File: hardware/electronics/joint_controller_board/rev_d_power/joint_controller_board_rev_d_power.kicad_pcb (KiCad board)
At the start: 2 copper layers, 40 x 60 mm, 19 parts, among them J1 J_IFACE, J2 J_PWR_IN_RAW, J3 J_PWR_CHAIN_RAW, J4 J_PWR_OUT_SW

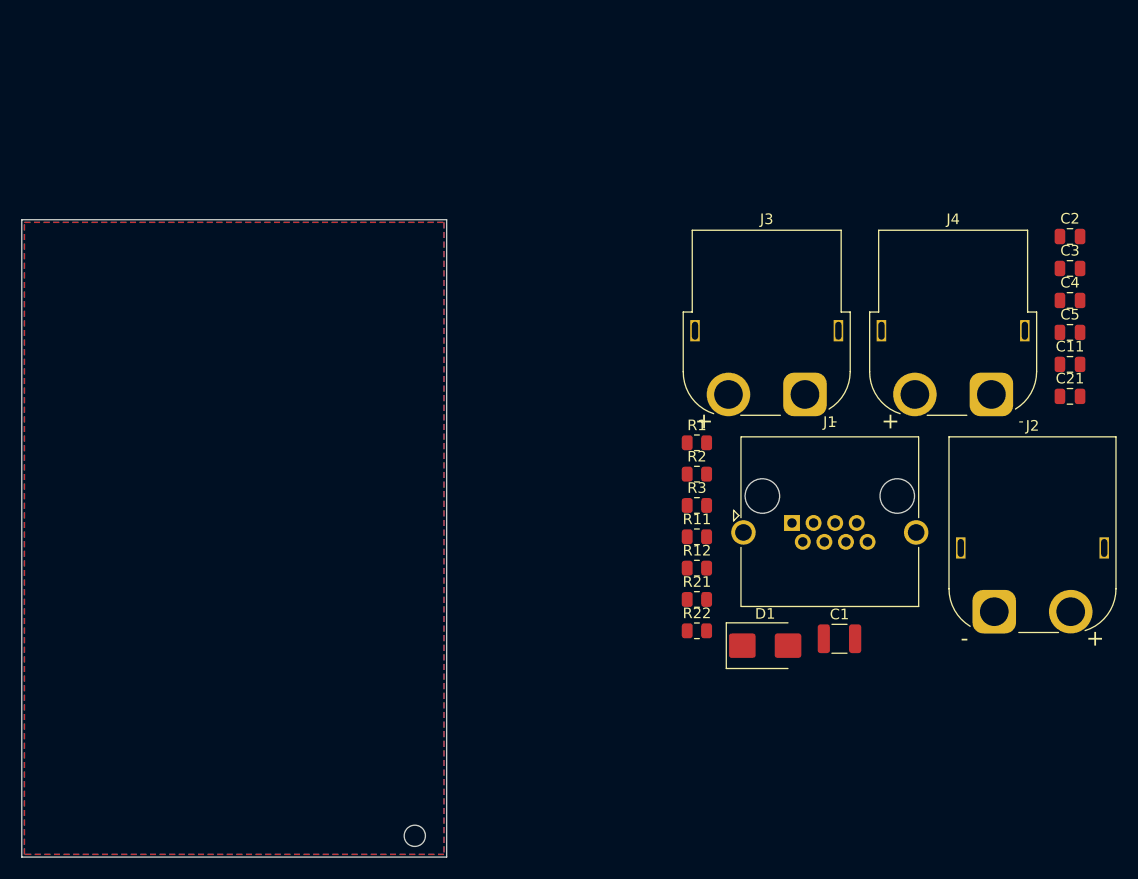
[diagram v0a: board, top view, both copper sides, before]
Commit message: feat: refine rev d power protection and buck
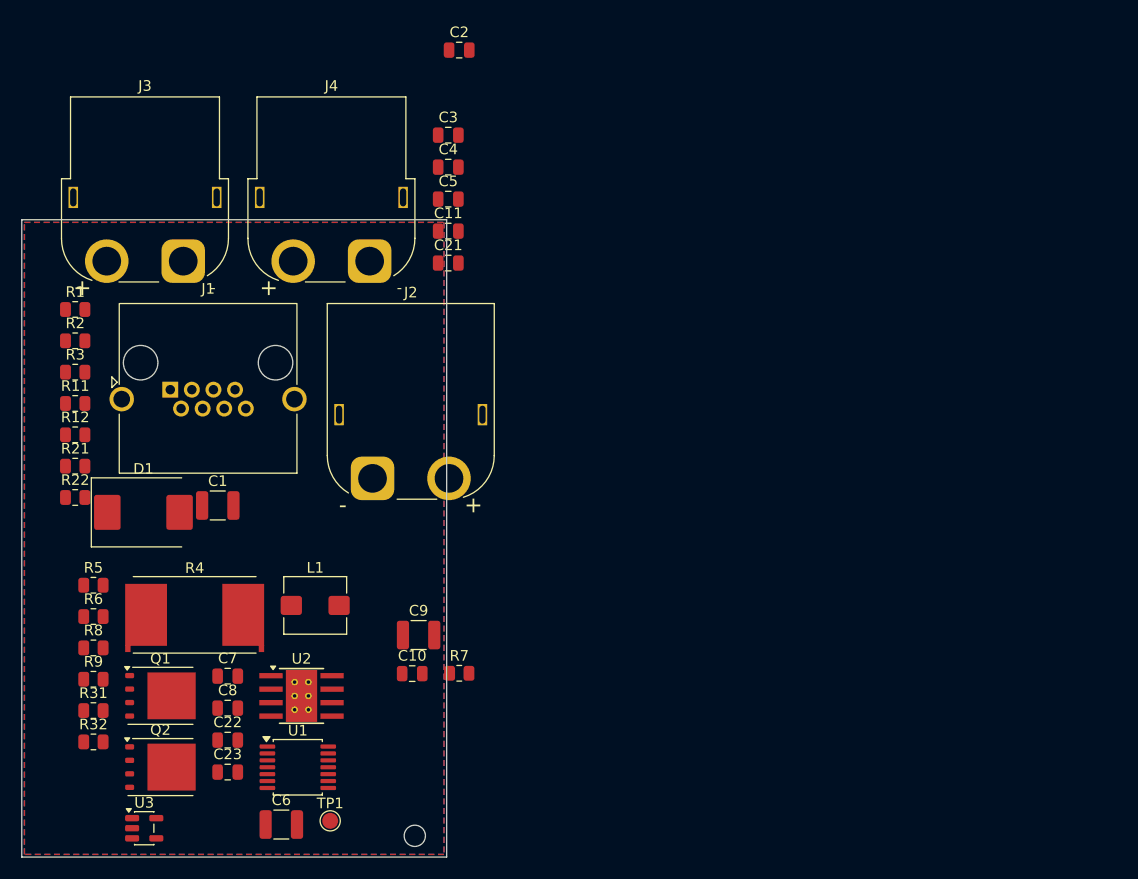
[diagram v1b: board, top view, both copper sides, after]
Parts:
- added C10: 10nF, Capacitor_SMD:C_0805_2012Metric, F.Cu at (156.8, 102.7)
- added C22: 47nF, Capacitor_SMD:C_0805_2012Metric, F.Cu at (139.4, 109.0)
- added C23: 100nF, Capacitor_SMD:C_0805_2012Metric, F.Cu at (139.4, 112.0)
- added C6: 4u7, Capacitor_SMD:C_1210_3225Metric, F.Cu at (144.4, 116.9)
- added C7: 1uF, Capacitor_SMD:C_0805_2012Metric, F.Cu at (139.4, 103.0)
- added C8: 100nF, Capacitor_SMD:C_0805_2012Metric, F.Cu at (139.4, 106.0)
- added C9: 22uF, Capacitor_SMD:C_1210_3225Metric, F.Cu at (157.4, 99.1)
- added L1: 15uH, Inductor_SMD:L_Bourns_SRP5030T, F.Cu at (147.6, 96.3)
- added Q1: BSC016N06NS, Package_TO_SOT_SMD:TDSON-8-1, F.Cu at (133.1, 104.8)
- added Q2: BSC016N06NS, Package_TO_SOT_SMD:TDSON-8-1, F.Cu at (133.1, 111.5)
- added R31: 220k, Resistor_SMD:R_0805_2012Metric, F.Cu at (126.7, 106.2)
- added R32: 10k, Resistor_SMD:R_0805_2012Metric, F.Cu at (126.7, 109.2)
- added R4: 1.25mOhm, Resistor_SMD:R_Shunt_Vishay_WSR2_WSR3_KelvinConnection, F.Cu at (136.3, 97.5)
- added R5: 10R, Resistor_SMD:R_0805_2012Metric, F.Cu at (126.7, 94.4)
- added R6: 10k, Resistor_SMD:R_0805_2012Metric, F.Cu at (126.7, 97.4)
- added R7: 10k, Resistor_SMD:R_0805_2012Metric, F.Cu at (161.2, 102.7)
- added R8: 100k, Resistor_SMD:R_0805_2012Metric, F.Cu at (126.7, 100.3)
- added R9: 24k9, Resistor_SMD:R_0805_2012Metric, F.Cu at (126.7, 103.3)
- added TP1: TP_IMON, TestPoint:TestPoint_Pad_D1.5mm, F.Cu at (149.0, 116.6)
- added U1: TPS2492PW, Package_SO:TSSOP-14_4.4x5mm_P0.65mm, F.Cu at (146.0, 111.5)
- added U2: LMR36520ADDA, Package_SO:Texas_HTSOP-8-1EP_3.9x4.9mm_P1.27mm_EP2.95x4.9mm_Mask2.4x3.1mm_ThermalVias, F.Cu at (146.3, 104.8)
- added U3: TLV75533PDBV, Package_TO_SOT_SMD:SOT-23-5, F.Cu at (131.5, 117.3)
- C1: value 100uF -> 22uF
- D1: value SMBJ33CA -> SMCJ33A; footprint Diode_SMD:D_SMB -> Diode_SMD:D_SMC
- R11, R21: value 68k -> 82k
- moved C2 60.1 mm to (161.2, 44.0)
- moved C1 59.9 mm to (138.4, 86.9)
- moved C11 59.9 mm to (160.2, 61.1)
- moved C21 59.9 mm to (160.2, 64.1)
- moved C3 59.9 mm to (160.2, 52.0)
- moved C4 59.9 mm to (160.2, 55.0)
- moved C5 59.9 mm to (160.2, 58.1)
- moved D1 59.9 mm to (131.5, 87.5)
- moved J1 59.9 mm to (134.0, 76.0)
- moved J2 59.9 mm to (153.0, 84.3)
- moved J3 59.9 mm to (135.2, 63.9)
- moved J4 59.9 mm to (152.8, 63.9)
- moved R1 59.9 mm to (125.0, 68.5)
- moved R11 59.9 mm to (125.0, 77.3)
- moved R12 59.9 mm to (125.0, 80.2)
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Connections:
- net /+3V3_AUX renamed +3V3_AUX
- net /24V_RAW renamed 24V_RAW
- C1 pad 2: /GND -> GND
- C11 pad 1: /VIN_POST_F1_MON -> VIN_POST_F1_MON
- C11 pad 2: /GND -> GND
- C2 pad 2: /GND -> GND
- C21 pad 1: /VOUT_POST_FET_MON -> VOUT_POST_FET_MON
- C21 pad 2: /GND -> GND
- C3 pad 1: /+5V_FROM_POWER -> +5V_FROM_POWER
- C3 pad 2: /GND -> GND
- C4 pad 2: /GND -> GND
- C5 pad 1: unconnected-(C5-Pad1) -> +5V_FROM_POWER
- C5 pad 2: /GND -> GND
- D1 pad 1: /GND -> GND
- J1 pad 1: unconnected-(J1-Pad1) -> +5V_FROM_POWER
- J1 pad 2: unconnected-(J1-Pad2) -> GND
- J1 pad 3: unconnected-(J1-Pad3) -> SAFETY_EN
- J1 pad 4: unconnected-(J1-Pad4) -> VIN_POST_F1_MON
- J1 pad 5: unconnected-(J1-Pad5) -> VOUT_POST_FET_MON
- J1 pad 6: unconnected-(J1-Pad6) -> PWRGD_N
- J1 pad 7: unconnected-(J1-Pad7) -> FAULT_N
- J1 pad 8: unconnected-(J1-Pad8) -> GND
- J1 pad SH: unconnected-(J1-PadSH) -> GND
- J2 pad 2: /GND -> GND
- J3 pad 2: /GND -> GND
- J4 pad 1: unconnected-(J4-Pin_1-Pad1) -> 24V_SW
- J4 pad 2: unconnected-(J4-Pin_2-Pad2) -> GND
- R1 pad 1: /SAFETY_EN -> SAFETY_EN
- R1 pad 2: /GND -> GND
- R11 pad 1: /24V_POST_F1 -> 24V_POST_F1
- R11 pad 2: /VIN_POST_F1_MON -> VIN_POST_F1_MON
- R12 pad 1: /VIN_POST_F1_MON -> VIN_POST_F1_MON
- R12 pad 2: /GND -> GND
- R2 pad 2: /PWRGD_N -> PWRGD_N
- R21 pad 1: /24V_SW -> 24V_SW
- R21 pad 2: /VOUT_POST_FET_MON -> VOUT_POST_FET_MON
- R22 pad 1: /VOUT_POST_FET_MON -> VOUT_POST_FET_MON
- R22 pad 2: /GND -> GND
- R3 pad 2: /FAULT_N -> FAULT_N

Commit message: feat(rev_d_power): multi-layer power zones + TPS2492 control hardening
Replace discrete power traces with multi-layer zones on 24V_RAW,
24V_POST_F1, 24V_SENSE_OUT, 24V_PASS_MID, 24V_SW: lower impedance
and better heat spreading on the 22A continuous path.

Schematic/control:
- C22 TIMER 47nF -> 10nF (~1.5ms) to keep Q1/Q2 inside SOA on hard short
- R6 47k VREF-PROG disables constant-power engine per TPS2492 DS p.8
- Remove TP1/R7/C10 IMON debug set; add no_connect on U1 pin 6
- BSC016N06NS symbol: drop duplicate drain pins (fix duplicate_pins ERC)

Layout/verification:
- GND zone continuity kept on both layers plus stitching vias
- 4 thermal vias on 24V_PASS_MID with F.Cu heat-spreader island
- 16-via array on Q2 -> J4 for 24V_SW cross-layer transition
- DRU exception for U2 HTSOP exposed pad mask bridges (standard TI layout)
- Reference text moved to Fab layer to clean silk overlap warnings

Result: ERC 0, DRC 0, 0 unconnected items. Ready for gerber export.
Signed-off-by: graceful-kinematics <info@aliahumanoid.com>
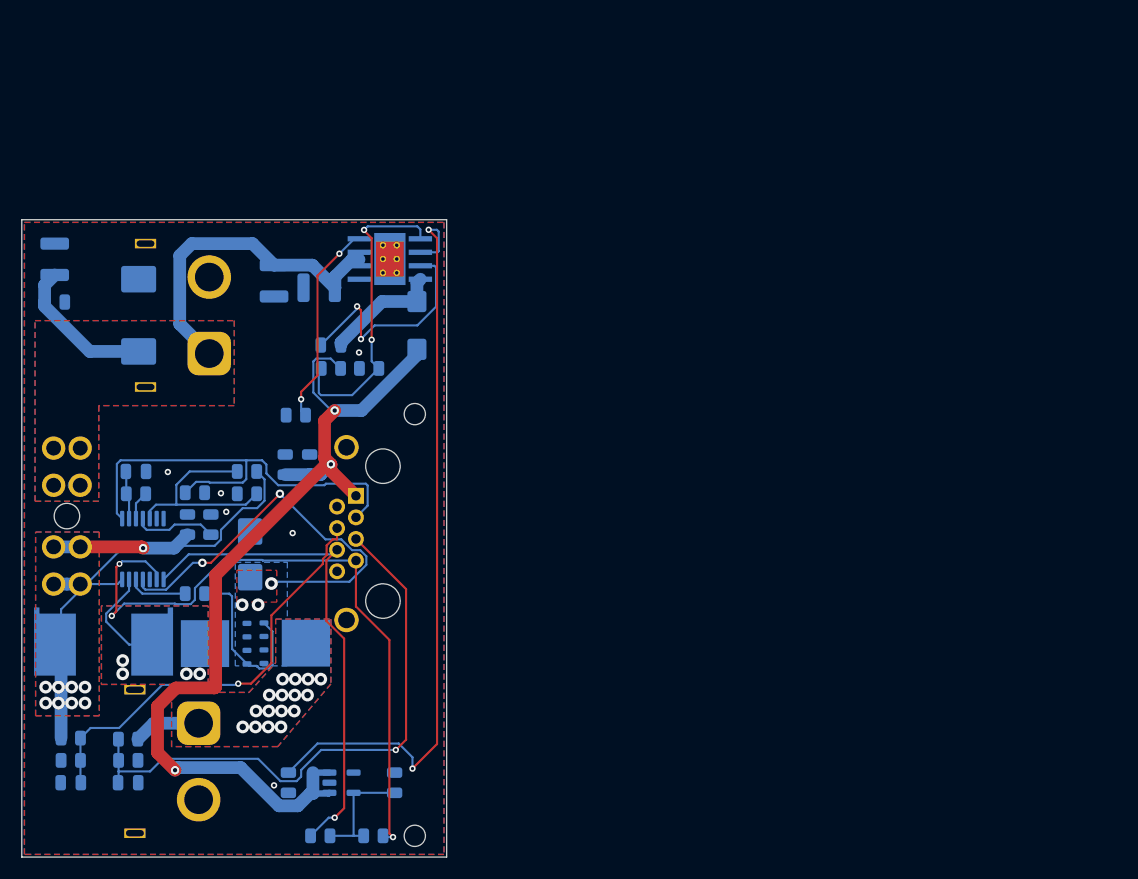
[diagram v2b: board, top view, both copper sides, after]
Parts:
- removed C10: 10nF, Capacitor_SMD:C_0805_2012Metric
- removed J3: J_PWR_CHAIN_RAW, Connector_AMASS:AMASS_XT60PW-F_1x02_P7.20mm_Horizontal
- removed R7: 10k, Resistor_SMD:R_0805_2012Metric
- removed TP1: TP_IMON, TestPoint:TestPoint_Pad_D1.5mm
- added C24: 100nF, Capacitor_SMD:C_0805_2012Metric, B.Cu at (135.6, 88.7)
- added D2: B560C-13-F, Diode_SMD:D_SMB, B.Cu at (141.5, 91.5)
- added F1: 30A, rev_d_power_footprints:FuseHolder_Blade_ATO_Littelfuse_FLR_178.6165, F.Cu at (125.5, 81.5)
- added R10: 0R, Resistor_SMD:R_0805_2012Metric, B.Cu at (145.8, 78.4)
- C1, C11, C2, C21, C3, C4, C5, C6, C7, C8, C9, D1, L1, Q1, Q2, R1, R11, R12, R2, R21, R22, R3, R31, R32, R4, R5, R8, R9, U1, U2, U3: moved to B.Cu
- C22: value 47nF -> 10nF; moved to B.Cu
- C23: value 100nF -> 470pF; moved to B.Cu
- R6: value 10k -> 47k; moved to B.Cu
- moved C11 62.9 mm to (124.6, 113.0), turned to 180 degrees
- moved C4 58.2 mm to (155.1, 113.0), turned to 90 degrees
- moved C21 57.5 mm to (130.0, 113.0)
- moved R2 52.0 mm to (148.1, 118.0), turned to 180 degrees
- moved R3 51.9 mm to (153.1, 118.0)
- moved C6 50.7 mm to (148.0, 66.4)
- moved J4 46.4 mm to (136.7, 107.4), turned to 90 degrees
- moved C2 44.9 mm to (123.1, 67.8)
- moved U2 42.0 mm to (154.7, 63.7)
- moved R9 39.1 mm to (152.7, 74.0)
- moved C9 36.0 mm to (143.8, 65.8), turned to 90 degrees
- moved C8 35.5 mm to (149.1, 71.8), turned to 180 degrees
- moved C3 34.6 mm to (144.8, 83.0), turned to 90 degrees
- moved R8 34.5 mm to (149.1, 74.0), turned to 180 degrees
- moved R11 31.5 mm to (124.6, 108.8)
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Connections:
- net Net-(Q1-G) renamed /HS_GATE
- D1 pad 1: GND -> 24V_RAW
- D1 pad 2: 24V_RAW -> GND
- R6 pad 2: GND -> Net-(U1-VREF)
- U1 pad 6: Net-(U1-IMON) -> unconnected-(U1-IMON-Pad6)
- U2 pad 4: unconnected-(U2-PG-Pad4) -> Net-(U2-PG)
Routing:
- net +5V_FROM_POWER: track 0.00 -> 92.3 mm, vias 0 -> 3
- net /U2_VCC: track 0.00 -> 71.1 mm, vias 0 -> 2
- net 24V_POST_F1: track 0.00 -> 70.3 mm, vias 0 -> 9
- net FAULT_N: track 0.00 -> 64.2 mm, vias 0 -> 3
- net VOUT_POST_FET_MON: track 0.00 -> 55.4 mm, vias 0 -> 1
- net PWRGD_N: track 0.00 -> 47.2 mm, vias 0 -> 1
- net 24V_RAW: track 0.00 -> 46.8 mm
- net SAFETY_EN: track 0.00 -> 42.3 mm
- net VIN_POST_F1_MON: track 0.00 -> 40.7 mm, vias 0 -> 1
- net 24V_PASS_MID: track 0.00 -> 38.5 mm, vias 0 -> 5
- net /U2_FB: track 0.00 -> 29.2 mm, vias 0 -> 2
- net /U2_BOOT: track 0.00 -> 21.8 mm, vias 0 -> 2
- net Net-(U1-OV): track 0.00 -> 19.6 mm
- net Net-(U2-PG): track 0.00 -> 19.3 mm, vias 0 -> 2
- net /HS_GATE: track 0.00 -> 16.6 mm
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- added copper zone on B.Cu, net 24V_PASS_MID
- added copper zone on F.Cu, net 24V_PASS_MID
- added copper zone on B.Cu, net 24V_POST_F1
- added copper zone on F.Cu, net 24V_POST_F1
- added copper zone on B.Cu, net 24V_RAW
- added copper zone on F.Cu, net 24V_RAW
- added copper zone on B.Cu, net 24V_SENSE_OUT
- added copper zone on F.Cu, net 24V_SENSE_OUT
- added copper zone on B.Cu, net 24V_SW
- added copper zone on F.Cu, net 24V_SW
- added copper zone on B.Cu, net GND
- added copper zone on F.Cu, net GND
- removed copper zone on B.Cu, net (none)
- removed copper zone on F.Cu, net (none)
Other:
- outline, holes or cut-outs redrawn

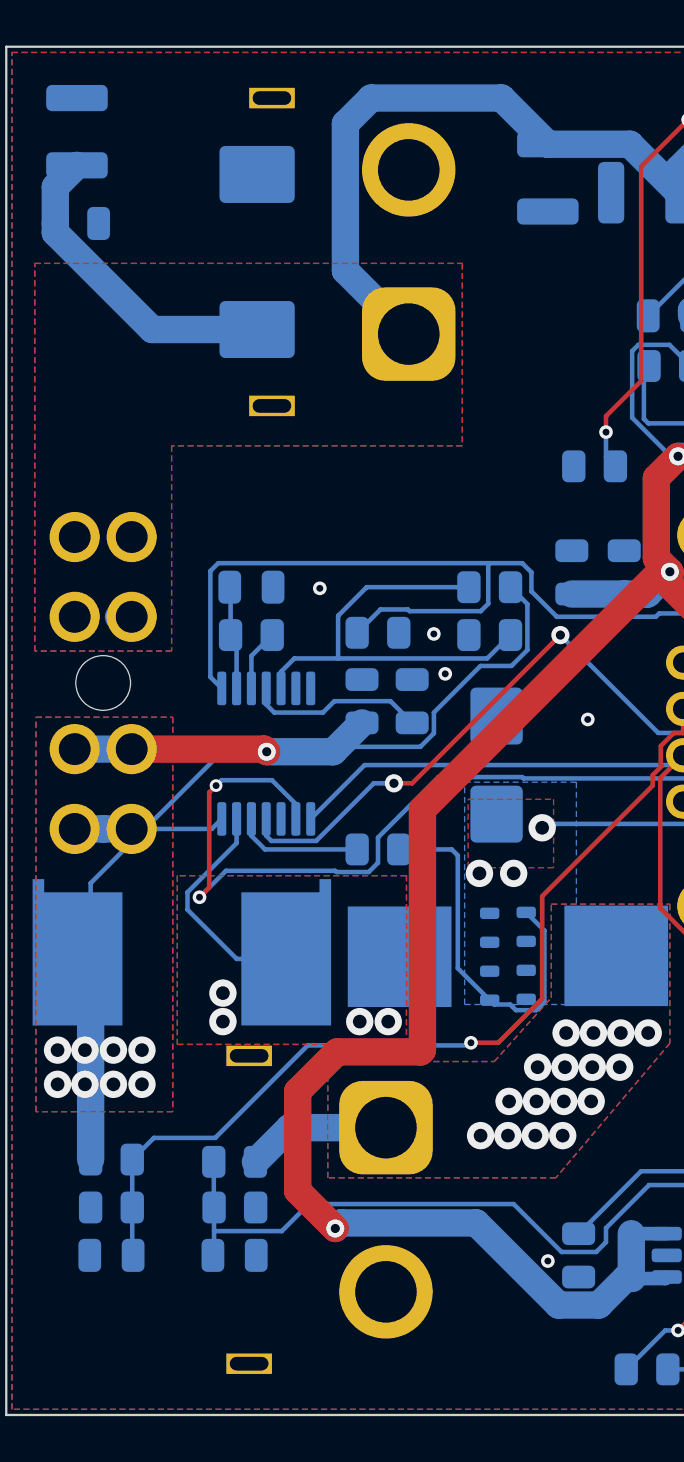
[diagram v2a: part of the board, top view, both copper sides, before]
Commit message: fix(rev_d_power): correct XT60 polarity pin assignment on J2/J4
Critical electrical fix: the AMASS XT60PW KiCad footprint convention
is pad 1 = negative (angled side), pad 2 = positive (flat side). The
schematic had the reversed assignment (pin 1 = 24V, pin 2 = GND) which
would have short-circuited the battery through the board on first power-up
since the XT60 housing is mechanically polarized and forces contact mating
to the physically marked + side.

Changes:
- J2 (XT60PW-M, 24V input): pin 1 -> GND, pin 2 -> 24V_RAW
- J4 (XT60PW-F, 24V switched output): pin 1 -> GND, pin 2 -> 24V_SW
- Re-loaded both footprints from stock KiCad library to restore correct
  pad local positions after polarity fix (pad 2 local X sign matches
  housing geometry: +7.2mm for M, -7.2mm for F)
- Moved refreshed silk elements to F.Fab layer on J2/J4 (matches the
  board-wide silk cleanup pattern used elsewhere)

Verification: rev_c (successfully fabricated) uses the same pin 1 = GND,
pin 2 = 24V assignment on XT60PW connectors, confirming the convention.

Result: ERC 0, DRC 0 violations, 0 unconnected items.
Signed-off-by: graceful-kinematics <info@aliahumanoid.com>
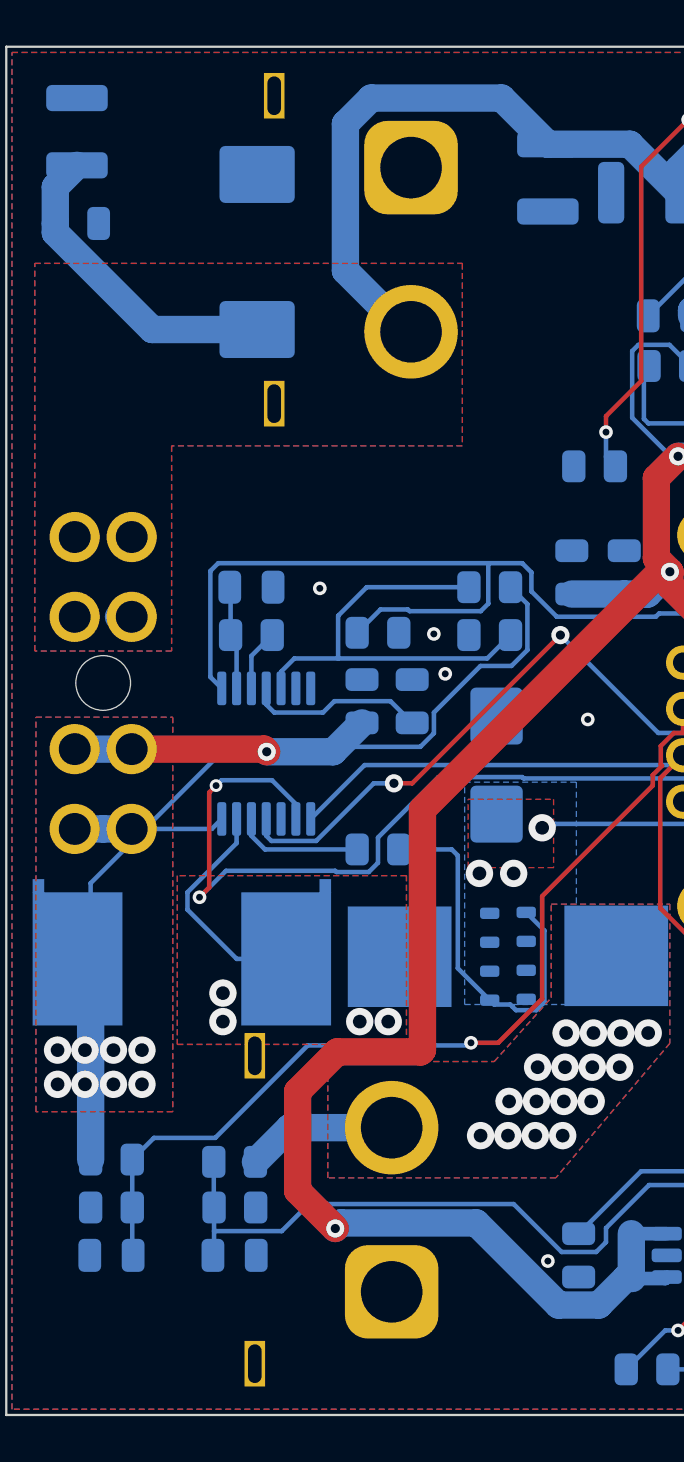
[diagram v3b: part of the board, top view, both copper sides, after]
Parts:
- J2: footprint Connector_AMASS:AMASS_XT60PW-M_1x02_P7.20mm_Horizontal -> AMASS_XT60PW-F_1x02_P7.20mm_Horizontal
- J4: footprint Connector_AMASS:AMASS_XT60PW-F_1x02_P7.20mm_Horizontal -> AMASS_XT60PW-M_1x02_P7.20mm_Horizontal
- moved J2 7.30 mm to (137.8, 65.3)
- moved J4 7.20 mm to (136.9, 114.6)
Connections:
- J2 pad 1: 24V_RAW -> GND
- J2 pad 2: GND -> 24V_RAW
- J4 pad 1: 24V_SW -> GND
- J4 pad 2: GND -> 24V_SW
